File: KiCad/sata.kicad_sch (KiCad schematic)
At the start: 3 parts

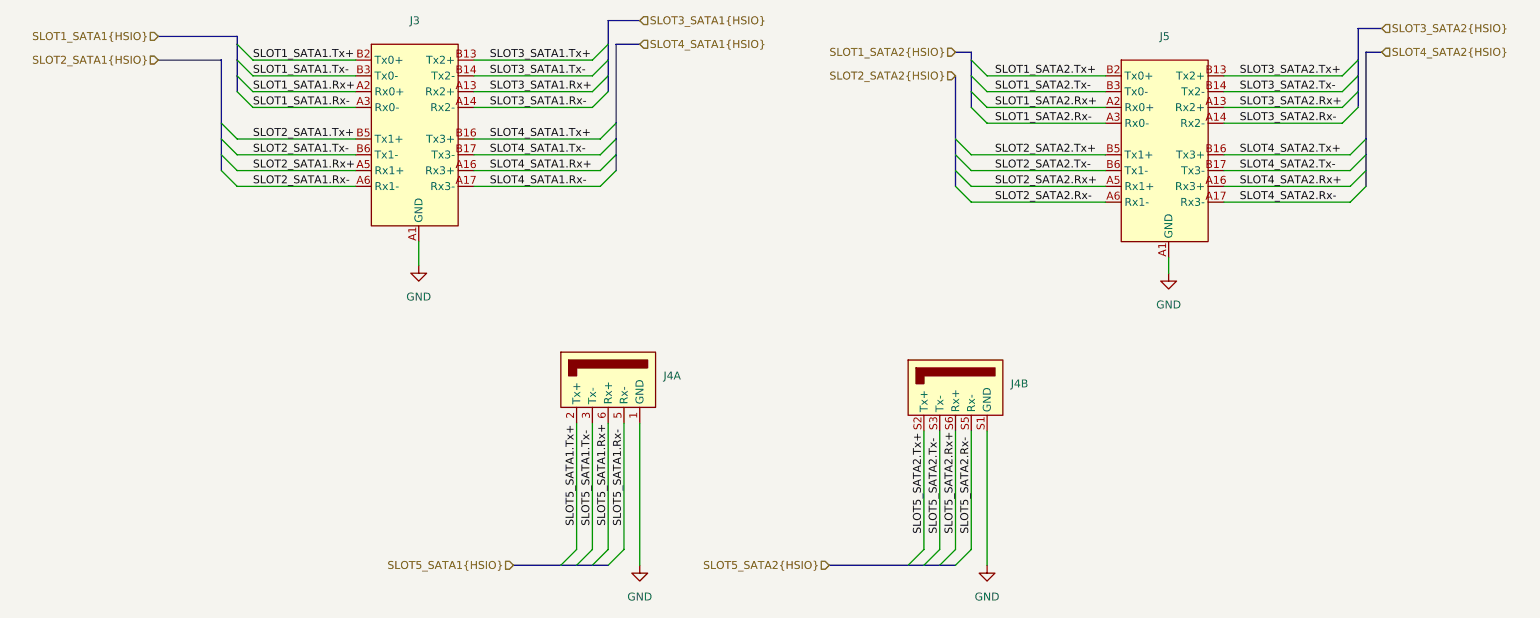
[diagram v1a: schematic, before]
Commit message: Add USB Type E Header Footprint
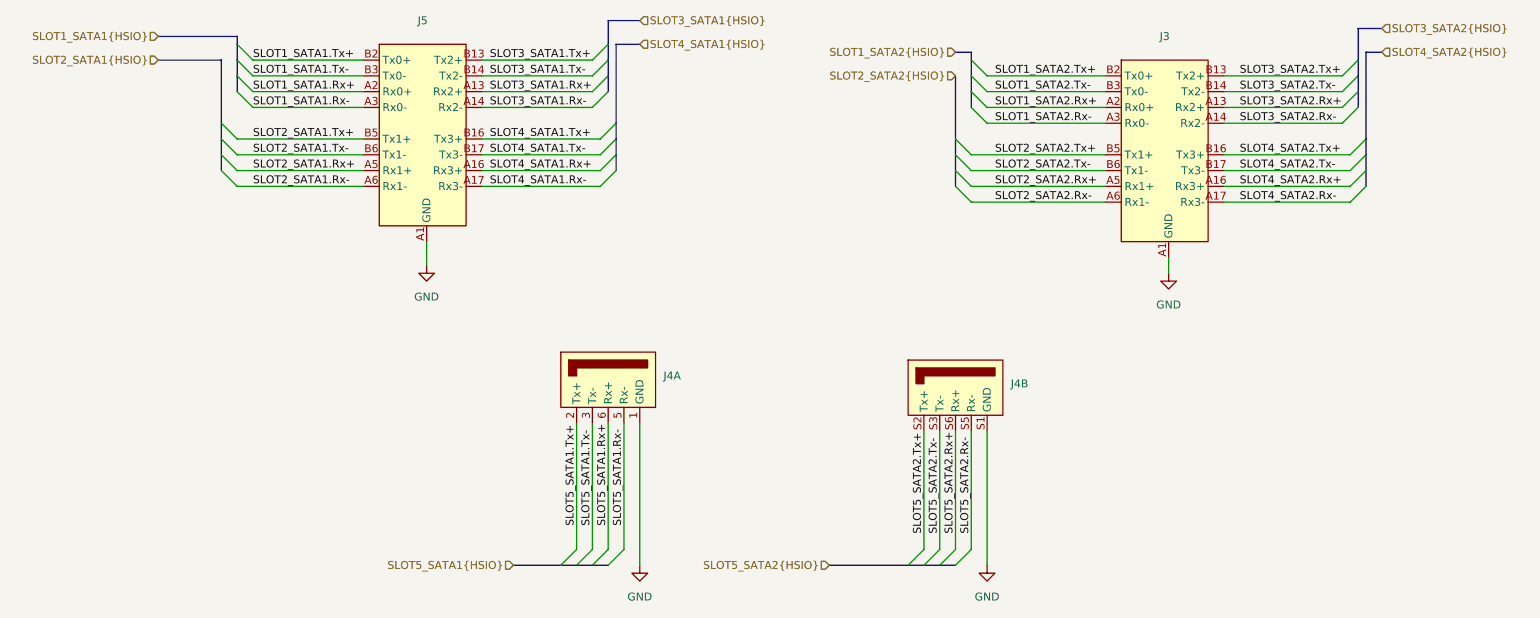
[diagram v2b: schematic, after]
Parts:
- removed J3, J5: ~, symbol custom:SFF-8087
- removed J4: ~, symbol custom:SATA_x2_stacked
- added J3, J5: ~, symbol Custom:SFF-8087
- added J4: ~, symbol Custom:SATA_x2_stacked
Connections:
- net GND: now also J3.A1 (GND), J3.A12 (GND), J3.A15 (GND), J3.A18 (GND), J3.A4 (GND), J3.A7 (GND), J3.B1 (GND), J3.B12 (GND), J3.B15 (GND), J3.B18 (GND), J3.B4 (GND), J3.B7 (GND), J3.SH (GND), J4.1 (GND), J4.15 (GND), J4.16 (GND), J4.4 (GND), J4.7 (GND), J4.S1 (GND), J4.S4 (GND), J4.S7 (GND), J5.A1 (GND), J5.A12 (GND), J5.A15 (GND), J5.A18 (GND), J5.A4 (GND), J5.A7 (GND), J5.B1 (GND), J5.B12 (GND), J5.B15 (GND), J5.B18 (GND), J5.B4 (GND), J5.B7 (GND), J5.SH (GND)
- net SLOT1_SATA1.Rx+: now also J5.A2 (Rx0+)
- net SLOT1_SATA1.Rx-: now also J5.A3 (Rx0-)
- net SLOT1_SATA1.Tx+: now also J5.B2 (Tx0+)
- net SLOT1_SATA1.Tx-: now also J5.B3 (Tx0-)
- net SLOT1_SATA2.Rx+: now also J3.A2 (Rx0+)
- net SLOT1_SATA2.Rx-: now also J3.A3 (Rx0-)
- net SLOT1_SATA2.Tx+: now also J3.B2 (Tx0+)
- net SLOT1_SATA2.Tx-: now also J3.B3 (Tx0-)
- net SLOT2_SATA1.Rx+: now also J5.A5 (Rx1+)
- net SLOT2_SATA1.Rx-: now also J5.A6 (Rx1-)
- net SLOT2_SATA1.Tx+: now also J5.B5 (Tx1+)
- net SLOT2_SATA1.Tx-: now also J5.B6 (Tx1-)
- net SLOT2_SATA2.Rx+: now also J3.A5 (Rx1+)
- net SLOT2_SATA2.Rx-: now also J3.A6 (Rx1-)
- net SLOT2_SATA2.Tx+: now also J3.B5 (Tx1+)
- net SLOT2_SATA2.Tx-: now also J3.B6 (Tx1-)
- net SLOT3_SATA1.Rx+: now also J5.A13 (Rx2+)
- net SLOT3_SATA1.Rx-: now also J5.A14 (Rx2-)
- net SLOT3_SATA1.Tx+: now also J5.B13 (Tx2+)
- net SLOT3_SATA1.Tx-: now also J5.B14 (Tx2-)
- net SLOT3_SATA2.Rx+: now also J3.A13 (Rx2+)
- net SLOT3_SATA2.Rx-: now also J3.A14 (Rx2-)
- net SLOT3_SATA2.Tx+: now also J3.B13 (Tx2+)
- net SLOT3_SATA2.Tx-: now also J3.B14 (Tx2-)
- net SLOT4_SATA1.Rx+: now also J5.A16 (Rx3+)
- net SLOT4_SATA1.Rx-: now also J5.A17 (Rx3-)
- net SLOT4_SATA1.Tx+: now also J5.B16 (Tx3+)
- net SLOT4_SATA1.Tx-: now also J5.B17 (Tx3-)
- net SLOT4_SATA2.Rx+: now also J3.A16 (Rx3+)
- net SLOT4_SATA2.Rx-: now also J3.A17 (Rx3-)
- net SLOT4_SATA2.Tx+: now also J3.B16 (Tx3+)
- net SLOT4_SATA2.Tx-: now also J3.B17 (Tx3-)
- net SLOT5_SATA1.Rx+: now also J4.6 (Rx+)
- net SLOT5_SATA1.Rx-: now also J4.5 (Rx-)
- net SLOT5_SATA1.Tx+: now also J4.2 (Tx+)
- net SLOT5_SATA1.Tx-: now also J4.3 (Tx-)
- net SLOT5_SATA2.Rx+: now also J4.S6 (Rx+)
- net SLOT5_SATA2.Rx-: now also J4.S5 (Rx-)
- net SLOT5_SATA2.Tx+: now also J4.S2 (Tx+)
- net SLOT5_SATA2.Tx-: now also J4.S3 (Tx-)

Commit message: Add footprintss from LCSC
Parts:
- J3, J5: value ~ -> SFF-8087; footprint (none) -> EasyEDA2KiCAD:CONN-SMD_LD2136V-MCUL6
- J4: value ~ -> SATA; footprint (none) -> EasyEDA2KiCAD:CONN-TH_XUTS-0722-2070
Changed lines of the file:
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@@
 			)
 		)
-		(property "Value" "~"
+		(property "Value" "SFF-8087"
 			(at 92.075 62.23 0)
 			(effects
@@
 			)
 		)
-		(property "Footprint" ""
+		(property "Footprint" "EasyEDA2KiCAD:CONN-SMD_LD2136V-MCUL6"
 			(at 92.71 62.23 0)
 			(effects
@@
 			)
 		)
-		(property "Value" "~"
+		(property "Value" "SFF-8087"
 			(at 211.455 64.77 0)
 			(effects
@@
 			)
 		)
-		(property "Footprint" ""
+		(property "Footprint" "EasyEDA2KiCAD:CONN-SMD_LD2136V-MCUL6"
 			(at 212.09 64.77 0)
 			(effects
@@
 			)
 		)
-		(property "Value" "~"
+		(property "Value" "SATA"
 			(at 186.69 120.015 0)
 			(effects
@@
 			)
 		)
-		(property "Footprint" ""
+		(property "Footprint" "EasyEDA2KiCAD:CONN-TH_XUTS-0722-2070"
 			(at 177.8 113.03 0)
 			(effects
@@
 			)
 		)
-		(property "Value" "~"
+		(property "Value" "SATA"
 			(at 130.81 118.745 0)
 			(effects
@@
 			)
 		)
-		(property "Footprint" ""
+		(property "Footprint" "EasyEDA2KiCAD:CONN-TH_XUTS-0722-2070"
 			(at 121.92 111.76 0)
 			(effects

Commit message: Finish fixing footprints
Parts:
- renumbered J5 to J3, J3 to J4, J4 to J5
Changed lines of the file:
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@@
 		(dnp no)
 		(fields_autoplaced yes)
-		(property "Reference" "#PWR0111"
+		(property "Reference" "#PWR0116"
 			(at 182.88 153.67 0)
 			(effects
@@
 			(project ""
 				(path "/49abeb3a-c598-45a3-ba6b-595eb04f17a8/bfd1ee61-dc44-45a6-bff2-e5d6f196c61b"
-					(reference "#PWR0111")
+					(reference "#PWR0116")
 					(unit 1)
 				)
@@
 		(dnp no)
 		(fields_autoplaced yes)
-		(property "Reference" "J5"
+		(property "Reference" "J3"
 			(at 92.075 59.69 0)
 			(effects
@@
 			(project ""
 				(path "/49abeb3a-c598-45a3-ba6b-595eb04f17a8/bfd1ee61-dc44-45a6-bff2-e5d6f196c61b"
-					(reference "J5")
+					(reference "J3")
 					(unit 1)
 				)
@@
 		(dnp no)
 		(fields_autoplaced yes)
-		(property "Reference" "#PWR0112"
+		(property "Reference" "#PWR0114"
 			(at 212.09 106.68 0)
 			(effects
@@
 			(project ""
 				(path "/49abeb3a-c598-45a3-ba6b-595eb04f17a8/bfd1ee61-dc44-45a6-bff2-e5d6f196c61b"
-					(reference "#PWR0112")
+					(reference "#PWR0114")
 					(unit 1)
 				)
@@
 		(dnp no)
 		(fields_autoplaced yes)
-		(property "Reference" "J3"
+		(property "Reference" "J4"
 			(at 211.455 62.23 0)
 			(effects
@@
 			(project ""
 				(path "/49abeb3a-c598-45a3-ba6b-595eb04f17a8/bfd1ee61-dc44-45a6-bff2-e5d6f196c61b"
-					(reference "J3")
+					(reference "J4")
 					(unit 1)
 				)
@@
 		(dnp no)
 		(fields_autoplaced yes)
-		(property "Reference" "#PWR0109"
+		(property "Reference" "#PWR0113"
 			(at 92.71 105.41 0)
 			(effects
@@
 			(project ""
 				(path "/49abeb3a-c598-45a3-ba6b-595eb04f17a8/bfd1ee61-dc44-45a6-bff2-e5d6f196c61b"
-					(reference "#PWR0109")
+					(reference "#PWR0113")
 					(unit 1)
 				)
@@
 		(dnp no)
 		(fields_autoplaced yes)
-		(property "Reference" "J4"
+		(property "Reference" "J5"
 			(at 186.69 118.1099 0)
 			(effects
@@
 			(project ""
 				(path "/49abeb3a-c598-45a3-ba6b-595eb04f17a8/bfd1ee61-dc44-45a6-bff2-e5d6f196c61b"
-					(reference "J4")
+					(reference "J5")
 					(unit 2)
 				)
@@
 		(dnp no)
 		(fields_autoplaced yes)
-		(property "Reference" "#PWR0110"
+		(property "Reference" "#PWR0115"
 			(at 127 153.67 0)
 			(effects
@@
 			(project ""
 				(path "/49abeb3a-c598-45a3-ba6b-595eb04f17a8/bfd1ee61-dc44-45a6-bff2-e5d6f196c61b"
-					(reference "#PWR0110")
+					(reference "#PWR0115")
 					(unit 1)
 				)
@@
 		(dnp no)
 		(fields_autoplaced yes)
-		(property "Reference" "J4"
+		(property "Reference" "J5"
 			(at 130.81 116.8399 0)
 			(effects
@@
 			(project ""
 				(path "/49abeb3a-c598-45a3-ba6b-595eb04f17a8/bfd1ee61-dc44-45a6-bff2-e5d6f196c61b"
-					(reference "J4")
+					(reference "J5")
 					(unit 1)
 				)

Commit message: Begin making 2 module card version
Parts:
- removed J3, J4: SFF-8087, EasyEDA2KiCAD:CONN-SMD_LD2136V-MCUL6, symbol Custom:SFF-8087
- removed J5: SATA, EasyEDA2KiCAD:CONN-TH_XUTS-0722-2070, symbol Custom:SATA_x2_stacked
